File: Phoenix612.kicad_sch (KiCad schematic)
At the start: 0 parts

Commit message: Add AF Stage
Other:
- added sheet AF Amp (AF_amp.kicad_sch)

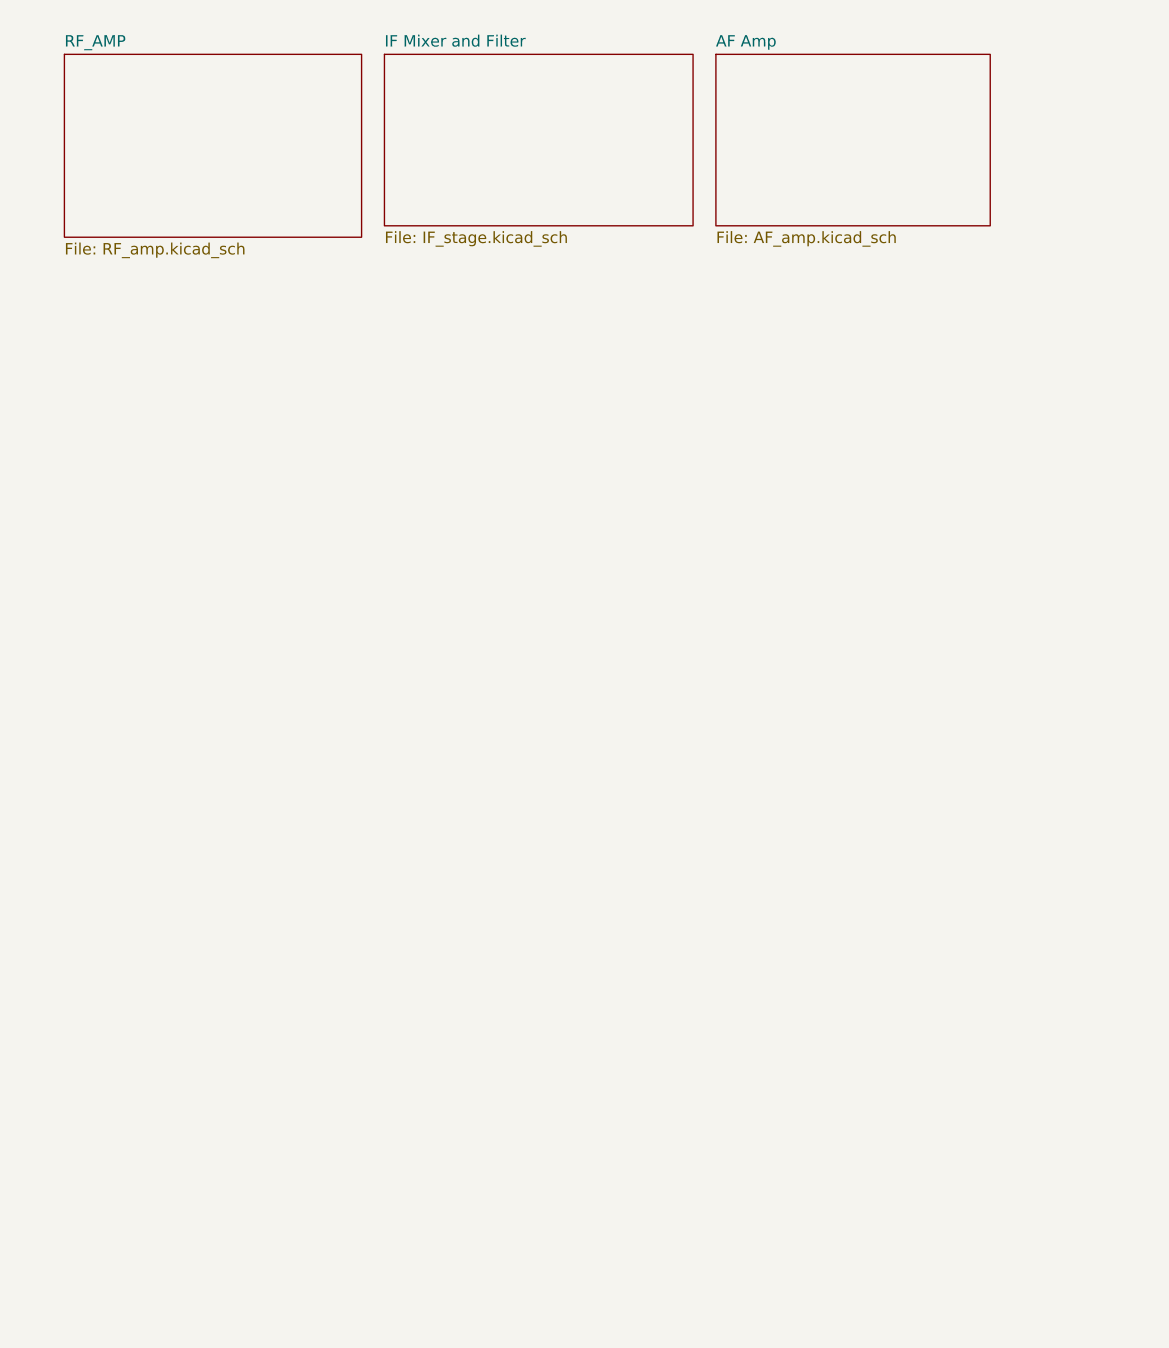
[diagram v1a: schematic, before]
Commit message: Continue Migration from D612
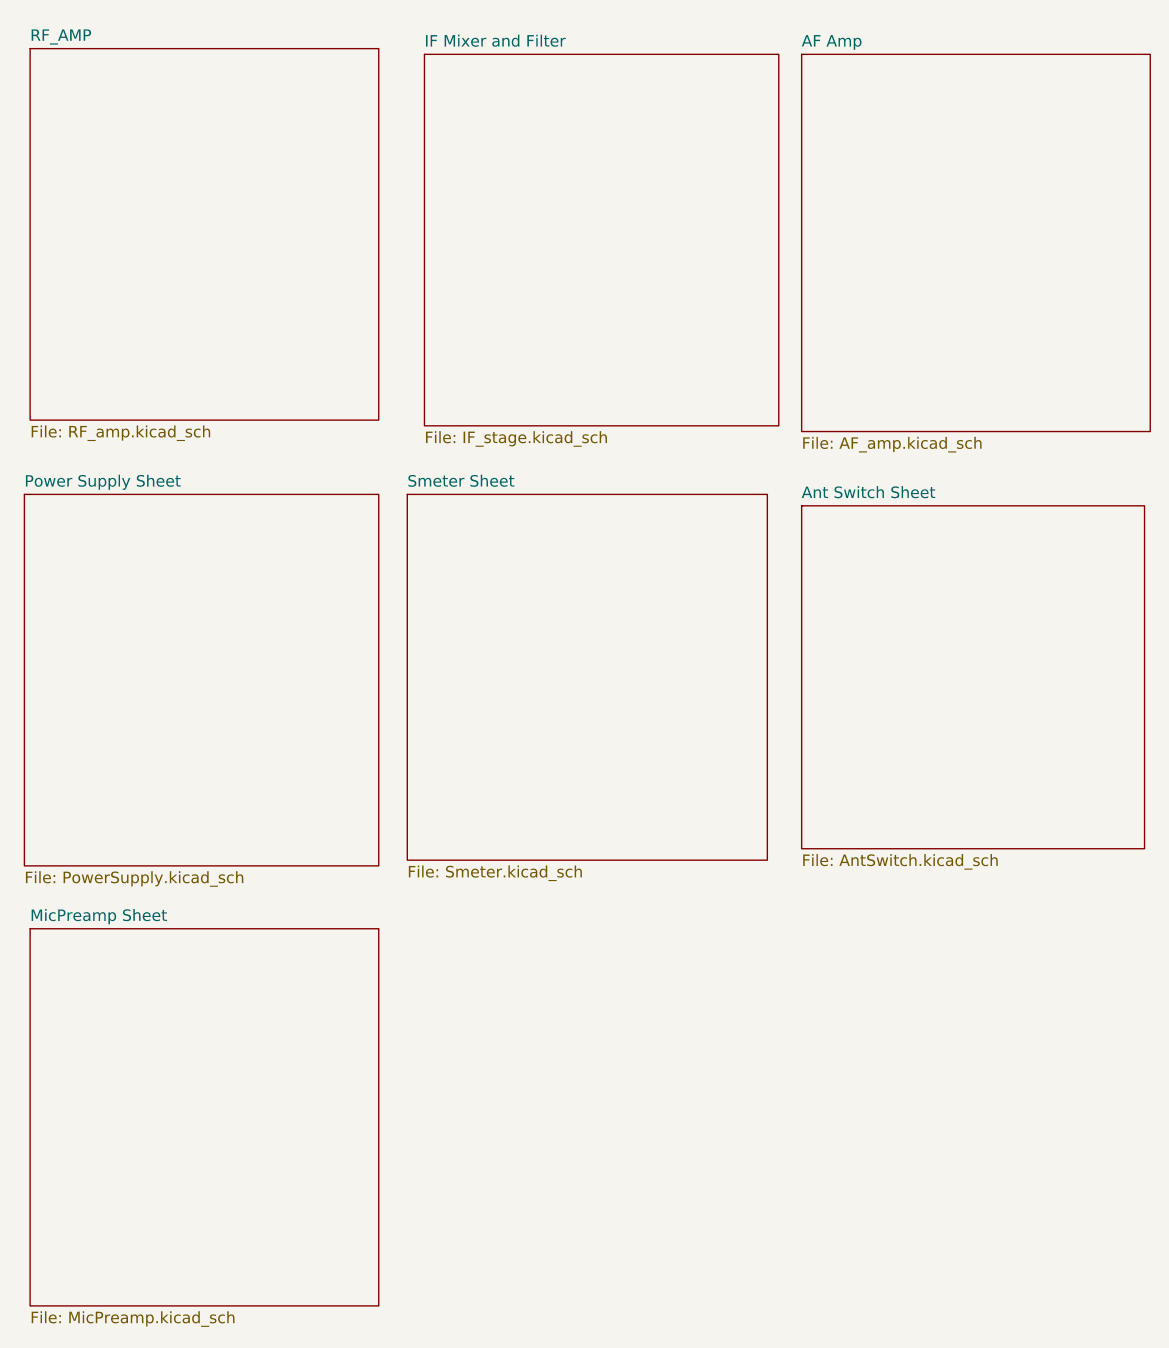
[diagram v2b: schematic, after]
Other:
- added sheet Ant Switch Sheet (AntSwitch.kicad_sch)
- added sheet MicPreamp Sheet (MicPreamp.kicad_sch)
- added sheet Power Supply Sheet (PowerSupply.kicad_sch)
- added sheet Smeter Sheet (Smeter.kicad_sch)

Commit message: Update
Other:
- added sheet PA Preamp (PA_Preamp.kicad_sch)
- added sheet Power Amp (PowerAmp.kicad_sch)
